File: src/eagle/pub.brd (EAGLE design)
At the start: 63.5 x 63.5 mm, 28 parts, among them IC1 PIC18F25K50, SW1 EC12E_SW

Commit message: Fixed typo in PICKIT header.
How did I not see it spelled as PICKKIT? Sheesh!
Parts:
- JP2: value PICKKIT -> PICKIT
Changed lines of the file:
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@@
 <attribute name="VALUE" x="4.445" y="21.59" size="1.27" layer="27" font="vector" rot="R270"/>
 </element>
-<element name="JP2" library="pub" package="1X06/90" value="PICKKIT" x="2.54" y="45.72" smashed="yes" rot="R90">
+<element name="JP2" library="pub" package="1X06/90" value="PICKIT" x="2.54" y="45.72" smashed="yes" rot="R90">
 <attribute name="NAME" x="3.81" y="37.465" size="1.27" layer="25" font="vector" ratio="10" rot="R180"/>
 <attribute name="VALUE" x="4.445" y="48.26" size="1.27" layer="27" font="vector" rot="R270"/>

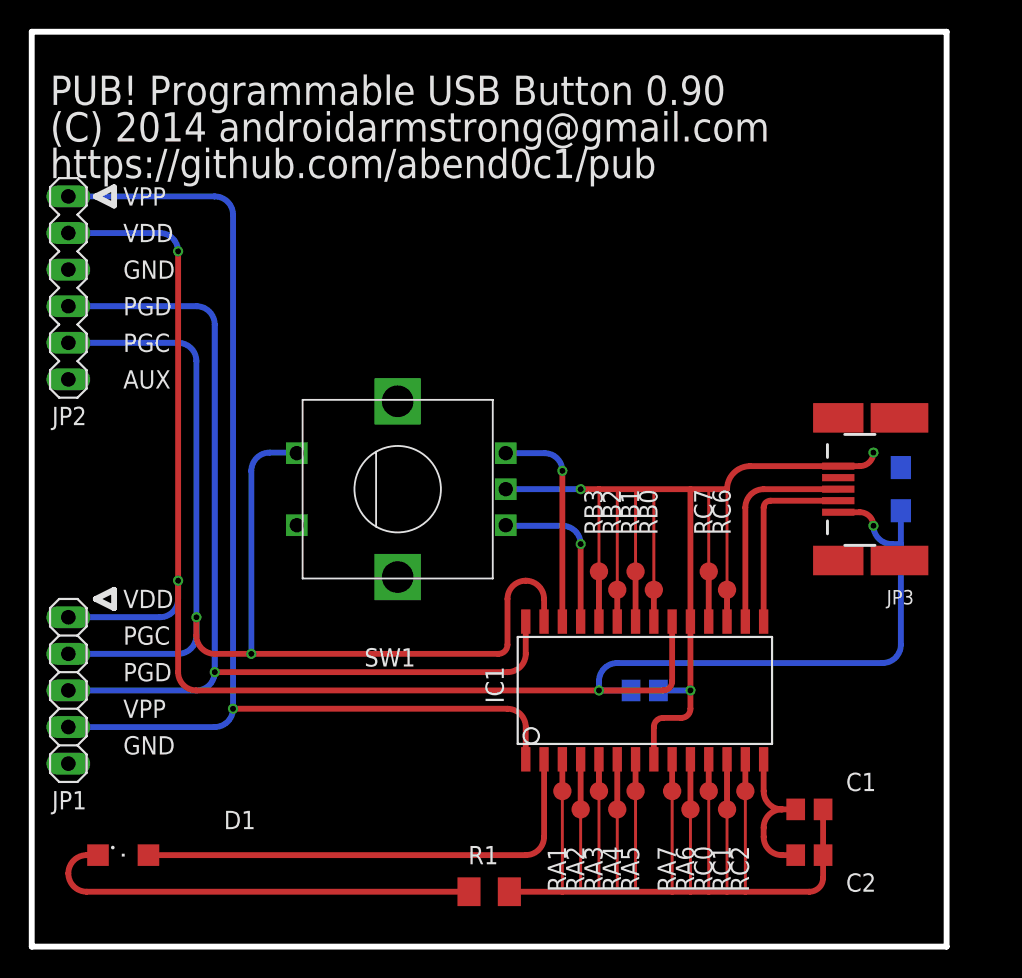
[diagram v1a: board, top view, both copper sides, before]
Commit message: Updated PCB art
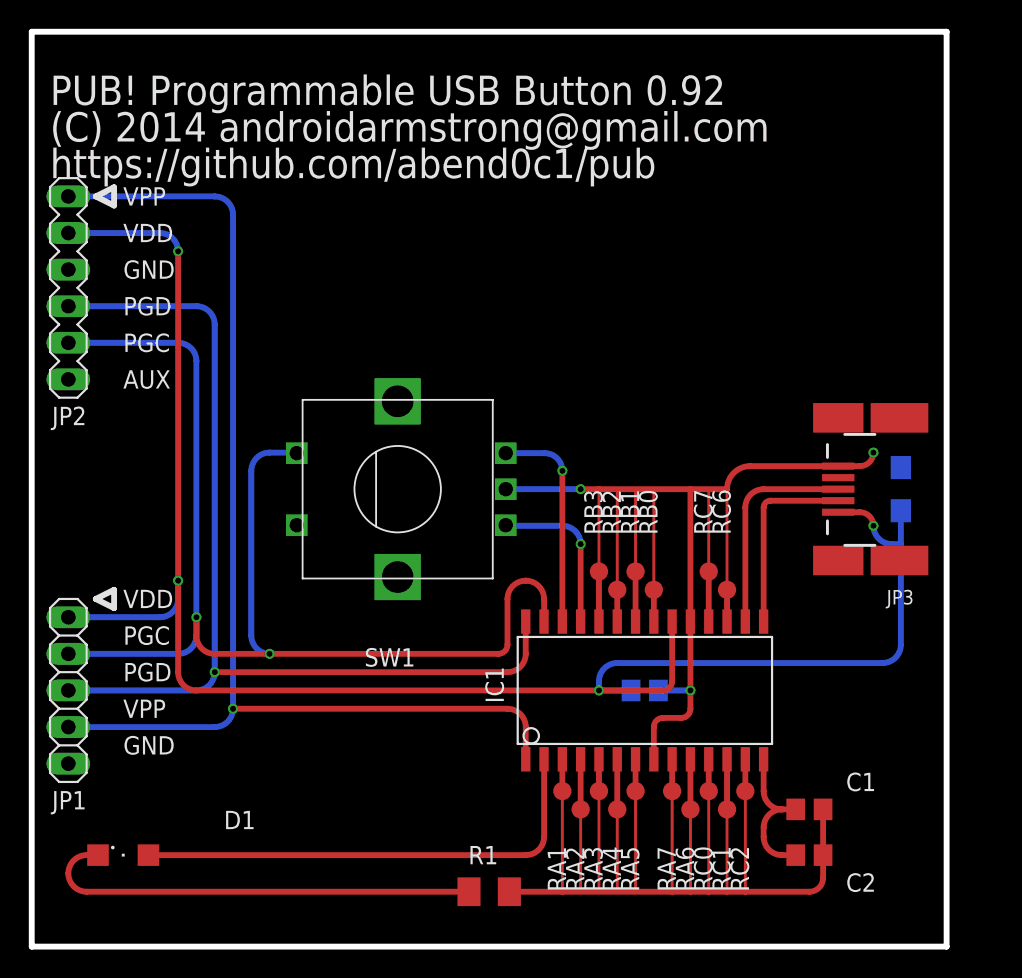
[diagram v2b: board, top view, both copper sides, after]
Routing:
- net N$8: track 86.3 -> 86.8 mm
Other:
- board text added: "PUB! Programmable USB Button 0.92"
- board text removed: "PUB! Programmable USB Button 0.90"
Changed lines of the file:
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@@
 <rectangle x1="53.975" y1="28.575" x2="60.96" y2="34.925" layer="41"/>
 <rectangle x1="36.83" y1="5.08" x2="50.8" y2="13.97" layer="41"/>
-<text x="1.27" y="58.42" size="2.032" layer="121" font="vector">PUB! Programmable USB Button 0.90</text>
+<text x="1.27" y="58.42" size="2.032" layer="121" font="vector">PUB! Programmable USB Button 0.92</text>
 <text x="1.27" y="55.88" size="2.032" layer="121" font="vector">(C) 2014 androidarmstrong@gmail.com</text>
 <text x="1.27" y="53.34" size="2.032" layer="121" font="vector">https://github.com/abend0c1/pub</text>
@@
 <wire x1="33.02" y1="24.13" x2="33.02" y2="20.955" width="0.4064" layer="1"/>
 <wire x1="33.02" y1="20.955" x2="32.385" y2="20.32" width="0.4064" layer="1" curve="-90"/>
-<wire x1="32.385" y1="20.32" x2="15.24" y2="20.32" width="0.4064" layer="1"/>
+<wire x1="32.385" y1="20.32" x2="16.51" y2="20.32" width="0.4064" layer="1"/>
 <contactref element="JP2" pad="5"/>
 <contactref element="JP1" pad="2"/>
-<wire x1="15.24" y1="20.32" x2="12.7" y2="20.32" width="0.4064" layer="1"/>
+<wire x1="16.51" y1="20.32" x2="12.7" y2="20.32" width="0.4064" layer="1"/>
 <wire x1="2.54" y1="41.91" x2="10.16" y2="41.91" width="0.4064" layer="16"/>
 <wire x1="2.54" y1="20.32" x2="10.16" y2="20.32" width="0.4064" layer="16"/>
@@
 <wire x1="18.36" y1="34.29" x2="16.51" y2="34.29" width="0.4064" layer="16"/>
 <wire x1="16.51" y1="34.29" x2="15.24" y2="33.02" width="0.4064" layer="16" curve="90"/>
-<wire x1="15.24" y1="33.02" x2="15.24" y2="20.32" width="0.4064" layer="16"/>
-<via x="15.24" y="20.32" extent="1-16" drill="0.4064"/>
+<via x="16.51" y="20.32" extent="1-16" drill="0.4064"/>
+<wire x1="15.24" y1="33.02" x2="15.24" y2="21.59" width="0.4064" layer="16"/>
+<wire x1="15.24" y1="21.59" x2="16.51" y2="20.32" width="0.4064" layer="16" curve="90"/>
 </signal>
 <signal name="N$9">
